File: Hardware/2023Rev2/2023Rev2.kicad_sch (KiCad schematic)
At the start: 104 parts, among them J1 Conn_01x09, J2 Conn_01x09, J3 Conn_01x04, J4 Conn_01x03, J5 Conn_01x02, J6 Conn_02x03_Counter_Clockwise, J7 RJ45_LED_Shielded, J8 Conn_01x03, Q1 Q_NMOS_GDS, Q2 Q_NMOS_DGS, Q3 Q_NMOS_DGS, Q4 Q_NMOS_DGS, U1 Teensy4.1_DEV-16771, U10 LT1910, U2 BMS_Logic_Switch, U3 Opamp_Dual, U4 ACS758xCB-200B-PFF, U5 Opamp_Dual, U6 OKI, U7 Opamp_Dual, U8 Opamp_Dual, U9 TSR_1-2450

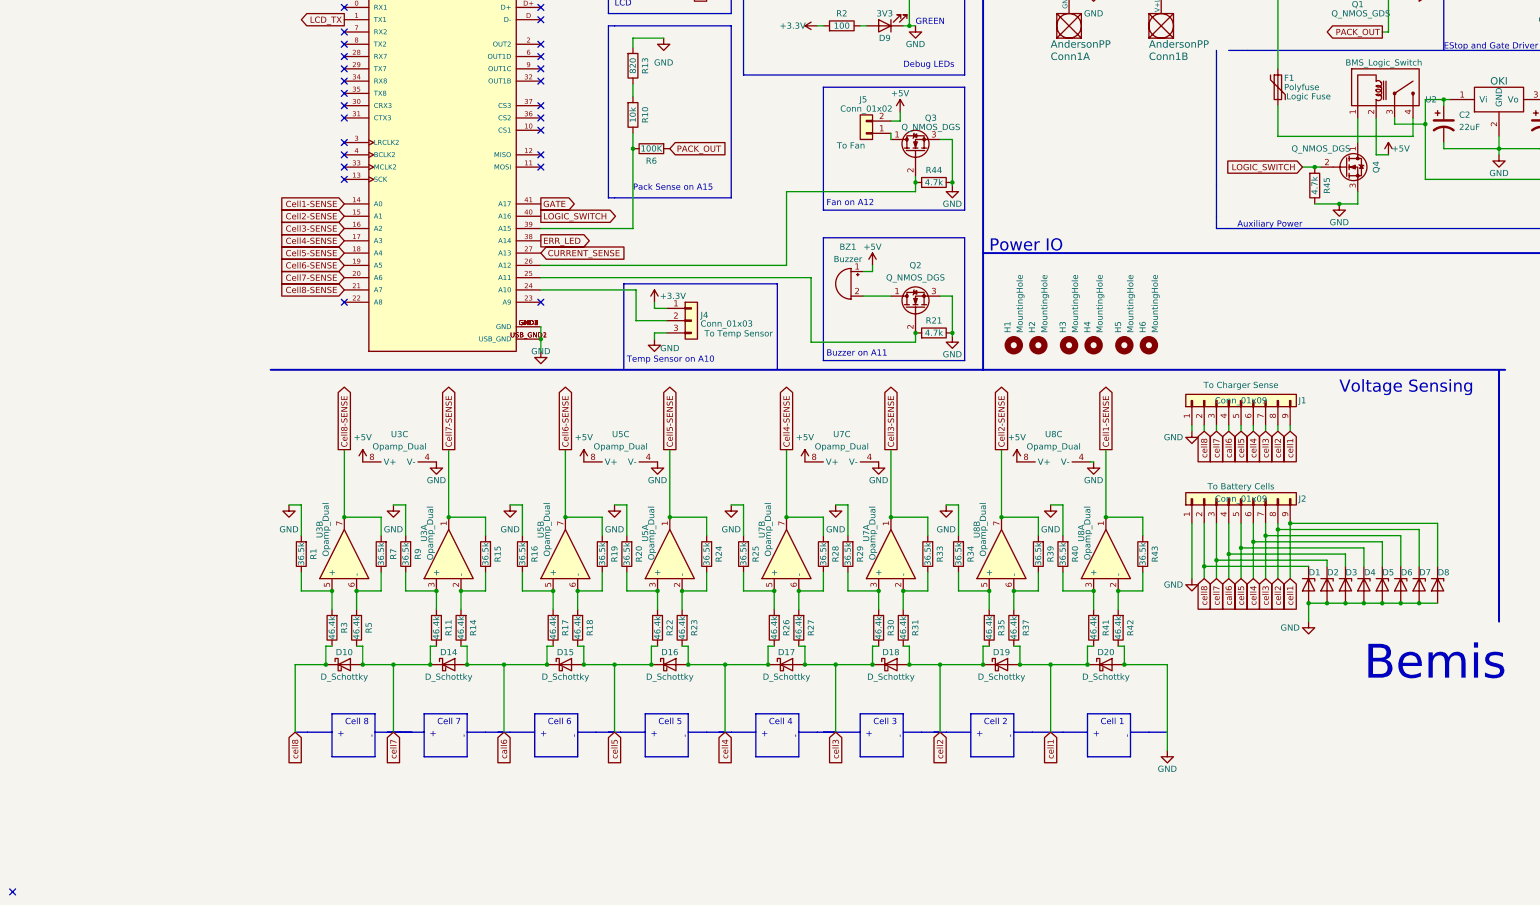
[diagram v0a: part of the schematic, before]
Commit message: Fixed N-Channel Transistor Footprints and OpAmp supply voltage
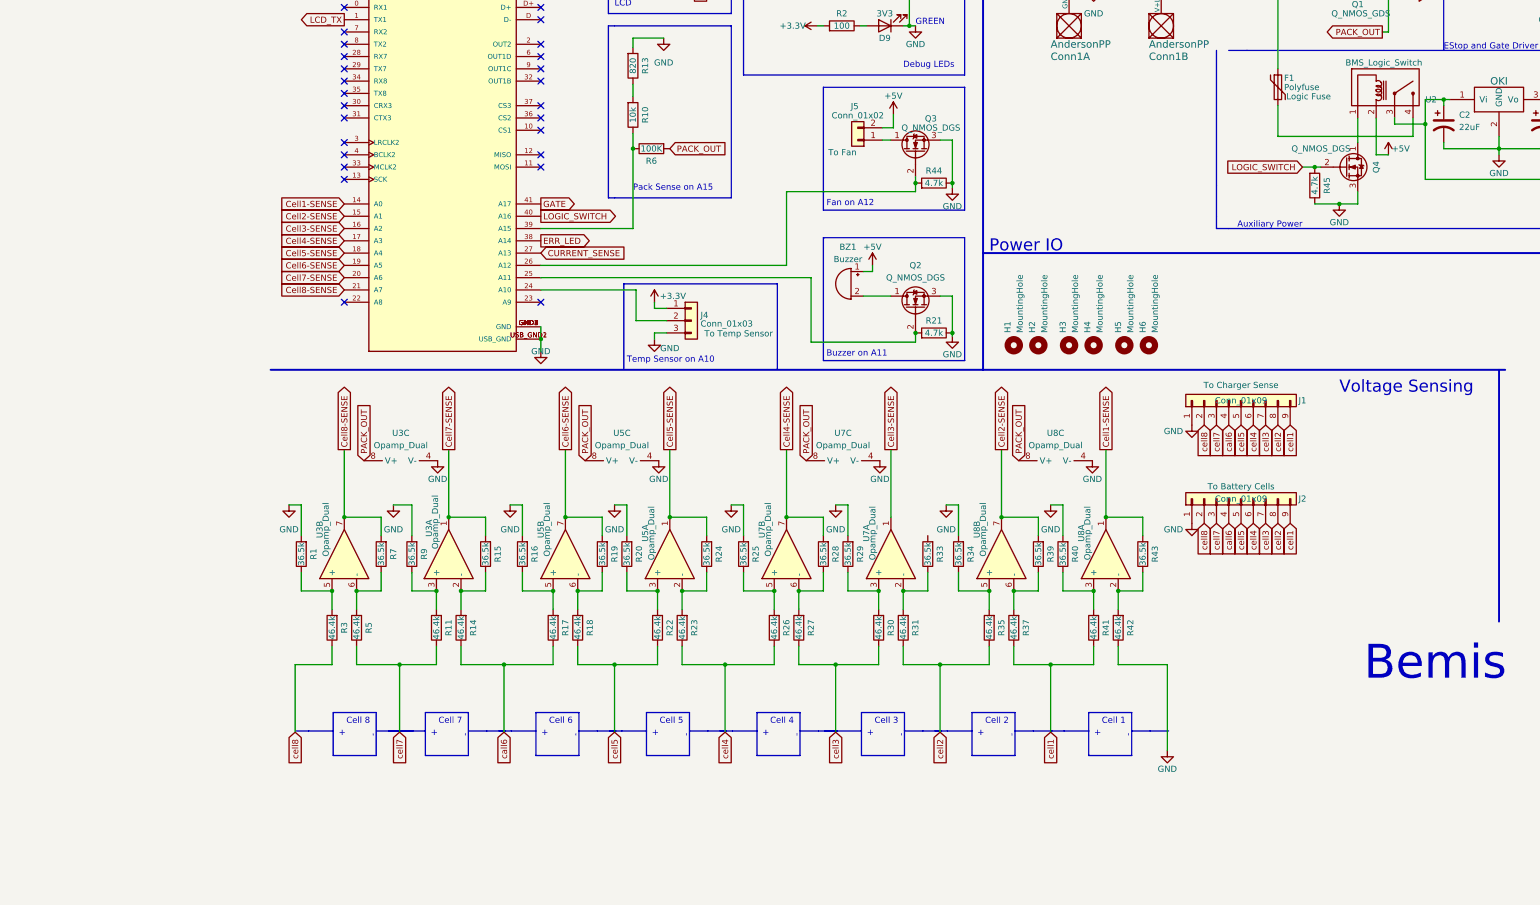
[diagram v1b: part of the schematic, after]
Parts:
- removed D1, D2, D3, D4, D5, D6, D7, D8: D_Zener, Package_TO_SOT_SMD:SOT-23, symbol Device:D_Zener
- removed D10, D14, D15, D16, D17, D18, D19, D20: D_Schottky, Diode_SMD:D_SOD-123, symbol Device:D_Schottky
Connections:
- net +5V: no longer U3.8 (V+), U5.8 (V+), U7.8 (V+), U8.8 (V+)
- net Cell3-SENSE: no longer R33.2
- net PACK_OUT: now also U3.8 (V+), U5.8 (V+), U7.8 (V+), U8.8 (V+)
- no-connect marks 44 -> 43
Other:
- company: MRDT - Drew Wellen, Cole Renken, Jesse Deuel -> MRDT - Drew Wellen, Jesse Deuel
- moved on the sheet: J5, R9

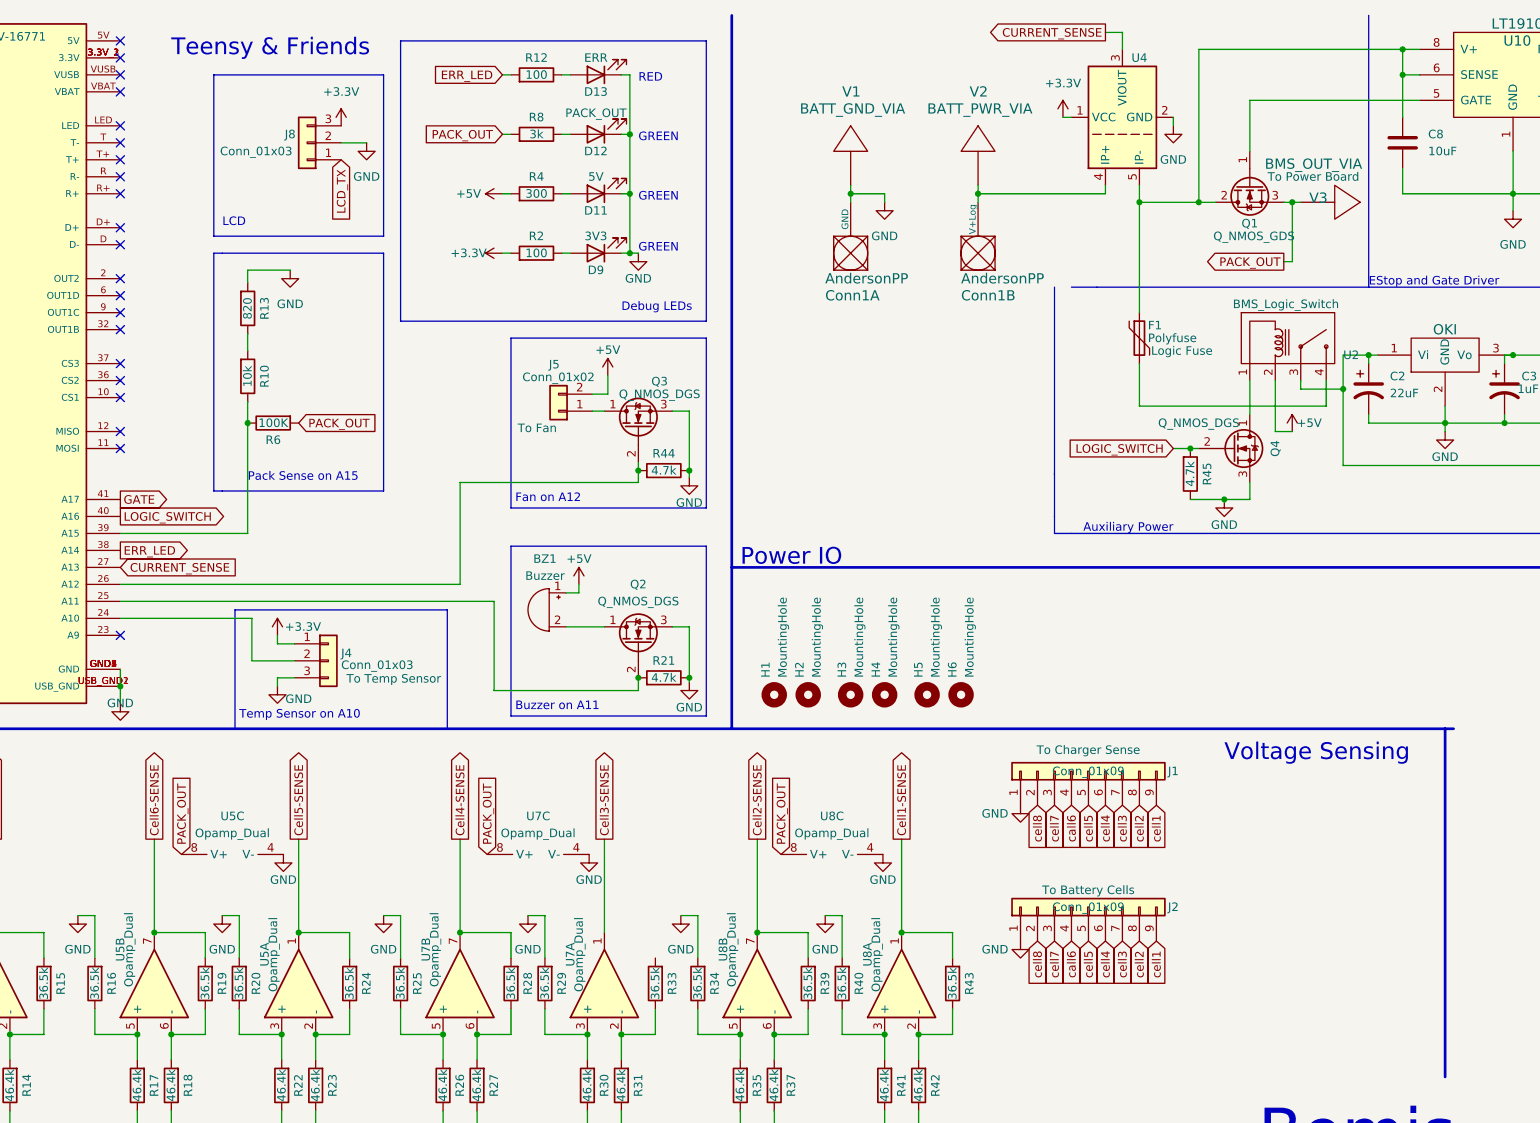
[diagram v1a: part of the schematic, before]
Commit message: Added LEDs to MOSFETS and changed 1st batt pin next to gnd
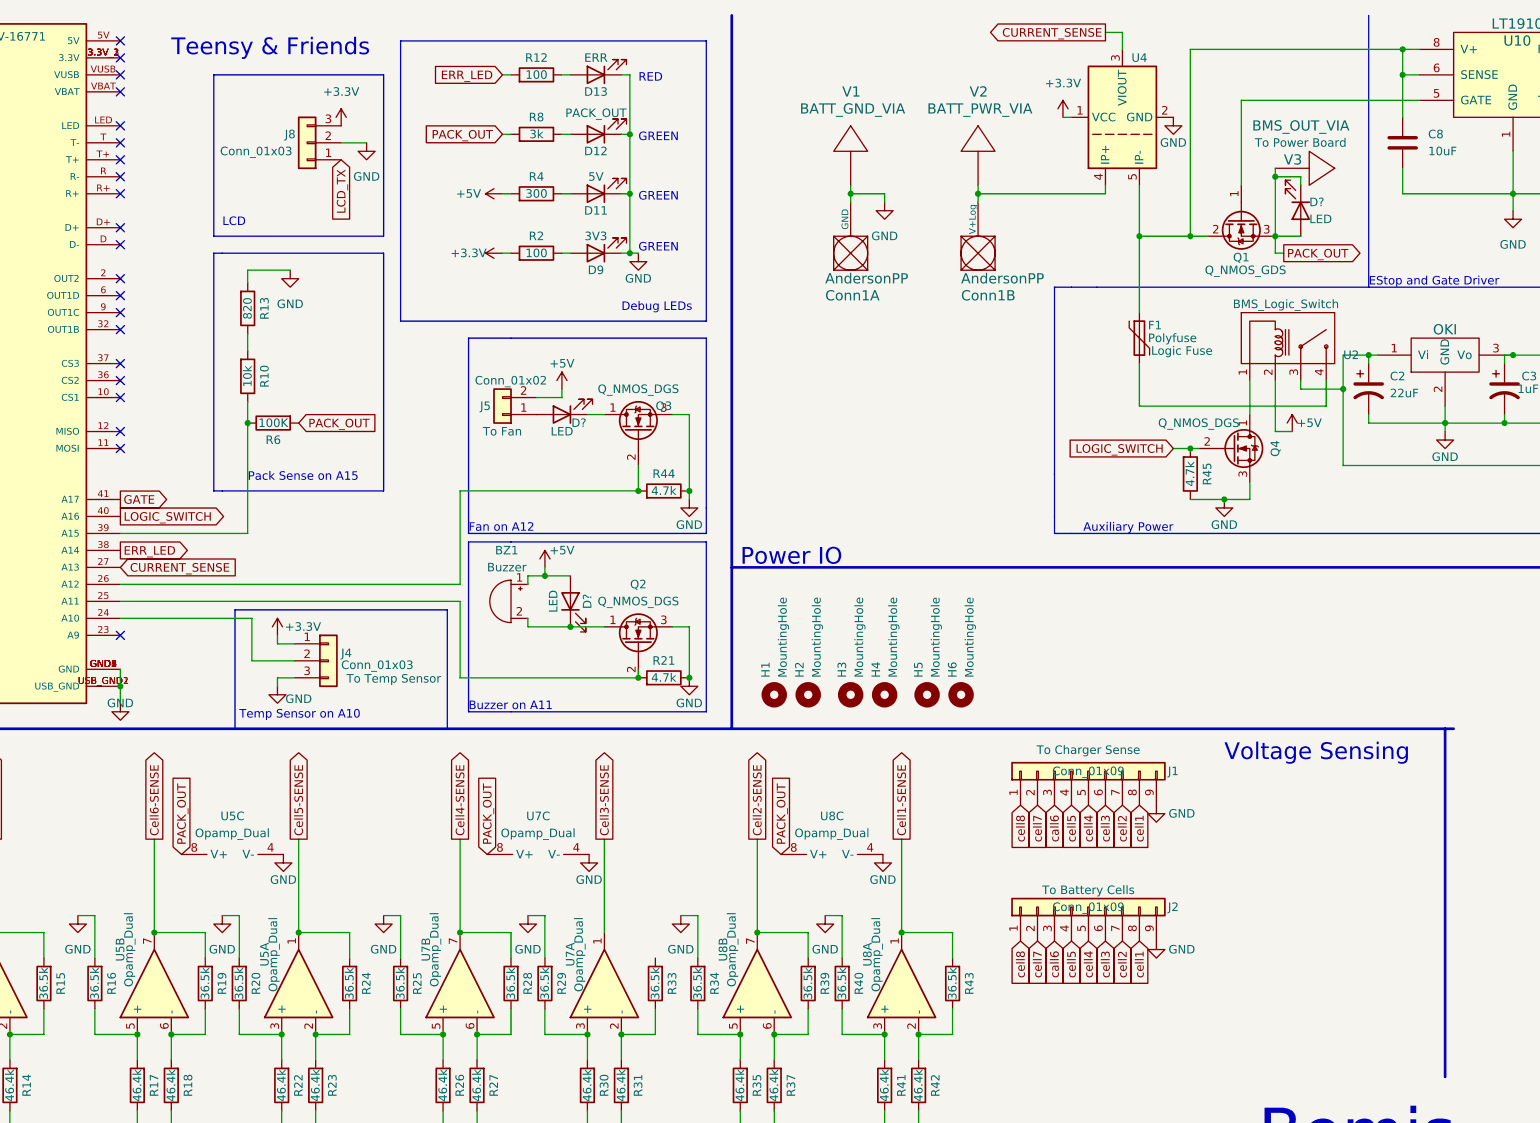
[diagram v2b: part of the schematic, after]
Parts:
- added D? (x3): LED, symbol Device:LED
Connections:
- net +5V: now also D?.2 (A)
- net GND: now also J1.9 (Pin_9), J2.9 (Pin_9); no longer J1.1 (Pin_1), J2.1 (Pin_1)
- net PACK_OUT: now also D?.1 (K), D?.2 (A)
- net call6: now also J1.3 (Pin_3), J2.3 (Pin_3); no longer J1.4 (Pin_4), J2.4 (Pin_4)
- net cell1: now also J1.8 (Pin_8), J2.8 (Pin_8); no longer J1.9 (Pin_9), J2.9 (Pin_9)
- net cell2: now also J1.7 (Pin_7), J2.7 (Pin_7); no longer J1.8 (Pin_8), J2.8 (Pin_8)
- net cell3: now also J1.6 (Pin_6), J2.6 (Pin_6); no longer J1.7 (Pin_7), J2.7 (Pin_7)
- net cell4: now also J1.5 (Pin_5), J2.5 (Pin_5); no longer J1.6 (Pin_6), J2.6 (Pin_6)
- net cell5: now also J1.4 (Pin_4), J2.4 (Pin_4); no longer J1.5 (Pin_5), J2.5 (Pin_5)
- net cell7: now also J1.2 (Pin_2), J2.2 (Pin_2); no longer J1.3 (Pin_3), J2.3 (Pin_3)
- net cell8: now also J1.1 (Pin_1), J2.1 (Pin_1); no longer J1.2 (Pin_2), J2.2 (Pin_2)
- net at Q3.1 (D): now also D?.1 (K); no longer J5.1 (Pin_1)
- net at BZ1.2 (+), Q2.1 (D): now also D?.1 (K)
- new net: D?.2 (A), J5.1 (Pin_1)
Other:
- moved on the sheet: BZ1, J5, Q1, Q3, R44, V3

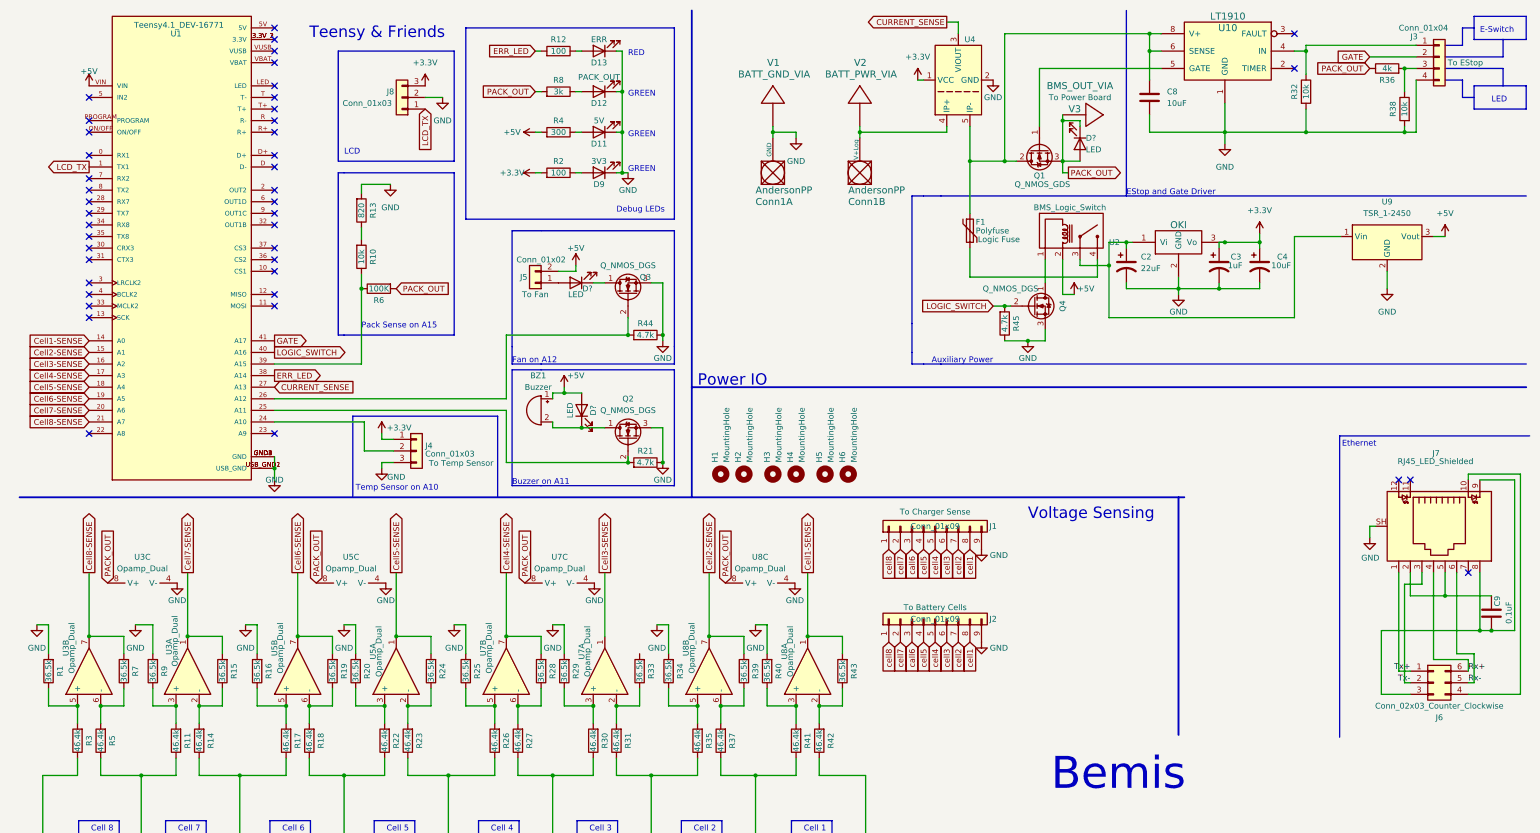
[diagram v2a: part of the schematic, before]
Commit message: Nearing completion of Rev2 Schematic
Started adding ethernet traces, Fixed resistor values, made Op-amp layouts consistent, and started adding LED indicators.
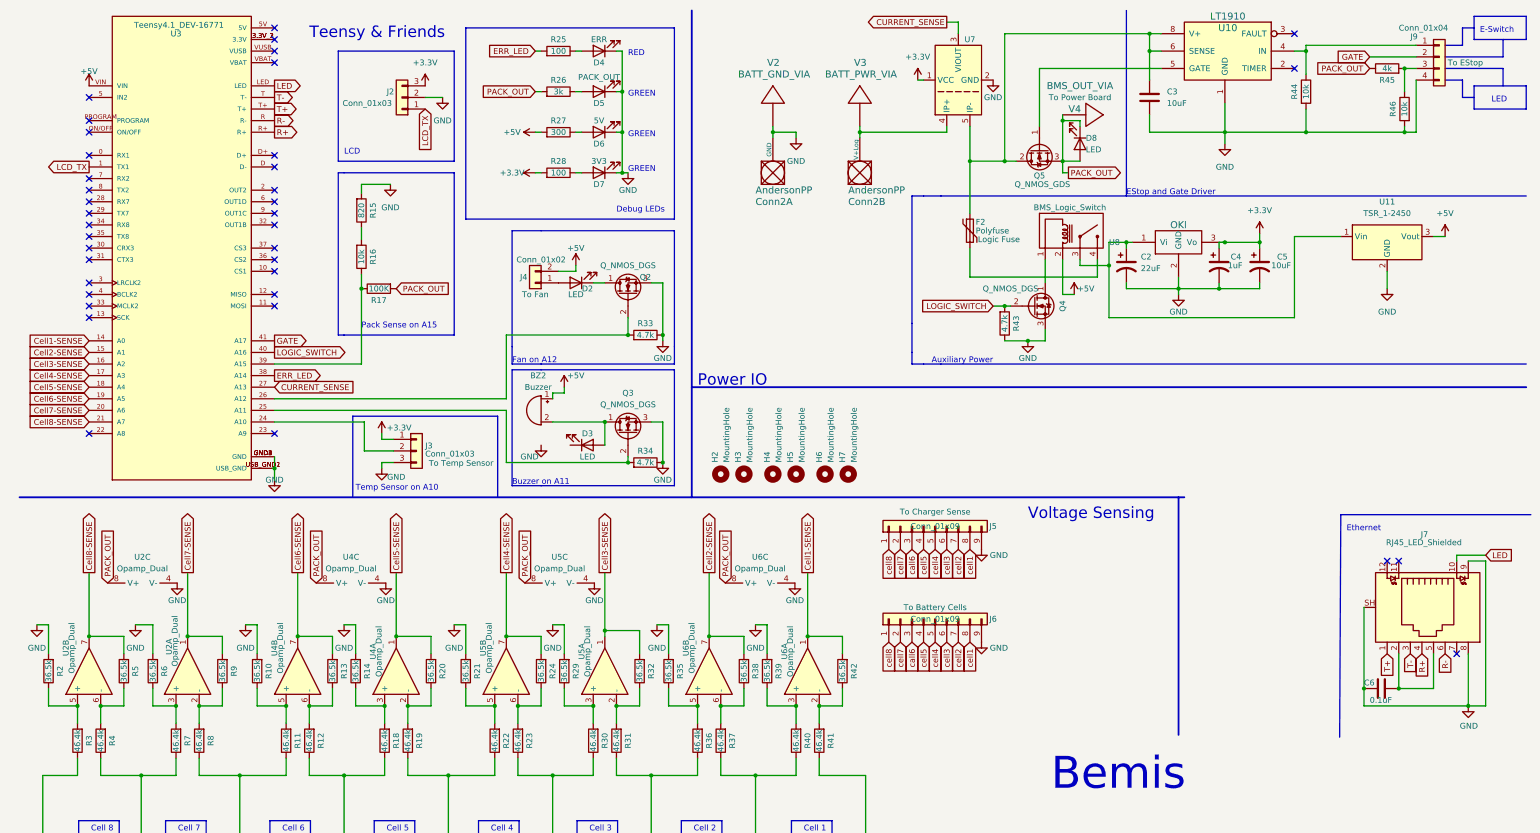
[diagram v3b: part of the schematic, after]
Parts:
- removed C9: 0.1uF, Capacitor_SMD:C_0603_1608Metric_Pad1.08x0.95mm_HandSolder, symbol Device:C
- removed J6: Conn_02x03_Counter_Clockwise, Connector_PinHeader_2.54mm:PinHeader_2x03_P2.54mm_Vertical, symbol Connector_Generic:Conn_02x03_Counter_Clockwise
- added C6: 0.1uF, Capacitor_SMD:C_0603_1608Metric_Pad1.08x0.95mm_HandSolder, symbol Device:C
- gave numbers to parts that had none: 3
- renumbered BZ1 to BZ2, C8 to C3, C3 to C4, C4 to C5, Conn1 to Conn2, D13 to D4, D12 to D5, D11 to D6, D9 to D7, F1 to F2, H1 to H2, H2 to H3, H3 to H4, H4 to H5, H5 to H6, H6 to H7, J8 to J2, J4 to J3, J5 to J4, J1 to J5, J2 to J6, J3 to J9, Q3 to Q2, Q2 to Q3, Q1 to Q5, R16 to R10, R17 to R11, R18 to R12, R19 to R13, R20 to R14, R13 to R15, R10 to R16, R6 to R17, R22 to R18, R23 to R19, R1 to R2, R24 to R20, R25 to R21, R26 to R22, R27 to R23, R28 to R24, R12 to R25, R8 to R26, R4 to R27, R2 to R28, R33 to R32, R44 to R33, R21 to R34, R34 to R35, R35 to R36, R39 to R38, R40 to R39, R5 to R4, R41 to R40, R42 to R41, R43 to R42, R45 to R43, R32 to R44, R36 to R45, R38 to R46, R7 to R5, R9 to R6, R11 to R7, R14 to R8, R15 to R9, U9 to U11, U3 to U2, U1 to U3, U5 to U4, U7 to U5, U8 to U6, U4 to U7, U2 to U8, U6 to U9, V1 to V2, V2 to V3, V3 to V4
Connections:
- net Rx+ is gone; now on net R+: J7.4
- net Rx- is gone; now on net R-: J7.6
- net Tx+ is gone; now on net T+: J7.1
- net Tx- is gone; now on net T-: J7.3
- net +5V: no longer D3.2 (A)
- net Cell3-SENSE: now also R32.2
- net GND: now also J7.8, J7.9, C6.2
- net at BZ2.2 (+), Q3.1 (D): now also D3.2 (A); no longer D3.1 (K)
- net LED: now reaches J7.10
- net LED: now also U3.LED
- net at J7.2, J7.5: now also C6.1
- net R-: now reaches U3.R (R-)
- net R+: now reaches U3.R+
- net T-: now reaches U3.T (T-)
- net T+: now reaches U3.T+
- no-connect marks 43 -> 38
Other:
- moved on the sheet: D3, Q3

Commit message: Finished schematic Rev2
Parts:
- removed D2, D3, D8: LED, symbol Device:LED
- added D?: Pack, LED_SMD:LED_0603_1608Metric_Pad1.05x0.95mm_HandSolder, symbol Device:LED
- added D?: Buzzer, LED_SMD:LED_0603_1608Metric_Pad1.05x0.95mm_HandSolder, symbol Device:LED
- added D?: Fan, LED_SMD:LED_0603_1608Metric_Pad1.05x0.95mm_HandSolder, symbol Device:LED
- added R? (x2): 75, symbol Device:R
- added R?: 1k, symbol Device:R
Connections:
- net GND: now also R?.1, R?.1, R?.1
- net PACK_OUT: now also D?.2 (A)
- net at Q2.1 (D): now also J4.1 (Pin_1), D?.2 (A)
- net at BZ2.2 (+), Q3.1 (D): now also D?.2 (A)
- net at Q5.1 (G), U10.5 (GATE): now also C3.1, F2.1, Q5.2 (D), U10.6 (SENSE), U10.8 (V+), U7.5 (IP-)
- new net: D?.1 (K), R?.2 (x3)
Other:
- moved on the sheet: Conn2A, Conn2B, Q5, U7, V2, V3
